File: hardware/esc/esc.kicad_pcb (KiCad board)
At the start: 2 copper layers, 214 parts, among them J1 TO_FC, J10 PHASE_A, J11 PHASE_B, J12 PHASE_C, J13 PHASE_A, J14 PHASE_B, J15 PHASE_C, J2 BAT_IN, J3 BAT_GND, J4 PHASE_A, J5 PHASE_B, J6 PHASE_C, J7 PHASE_A, J8 PHASE_B, J9 PHASE_C, Q1 NVTFWS003N04XMTAG, Q10 NVTFWS003N04XMTAG, Q11 NVTFWS003N04XMTAG, Q12 NVTFWS003N04XMTAG, Q13 NVTFWS003N04XMTAG, Q14 NVTFWS003N04XMTAG, Q15 NVTFWS003N04XMTAG, Q16 NVTFWS003N04XMTAG, Q17 NVTFWS003N04XMTAG, Q18 NVTFWS003N04XMTAG, Q19 NVTFWS003N04XMTAG, Q2 NVTFWS003N04XMTAG, Q20 NVTFWS003N04XMTAG, Q21 NVTFWS003N04XMTAG, Q22 NVTFWS003N04XMTAG, Q23 NVTFWS003N04XMTAG, Q24 NVTFWS003N04XMTAG, Q3 NVTFWS003N04XMTAG, Q4 NVTFWS003N04XMTAG, Q5 NVTFWS003N04XMTAG, Q6 NVTFWS003N04XMTAG, Q7 NVTFWS003N04XMTAG, Q8 NVTFWS003N04XMTAG, Q9 NVTFWS003N04XMTAG, U1 DRV8300DRGER, U10 DRV8300DRGER, U11 STM32G071K8U6, U12 INA180A1, U13 TPS56339DDC, U14 NCP59800BMNADJTAG, U2 STM32G071K8U6, U3 INA180A1, U4 DRV8300DRGER, U5 STM32G071K8U6, U6 INA180A1, U7 DRV8300DRGER, U8 STM32G071K8U6, U9 INA180A1

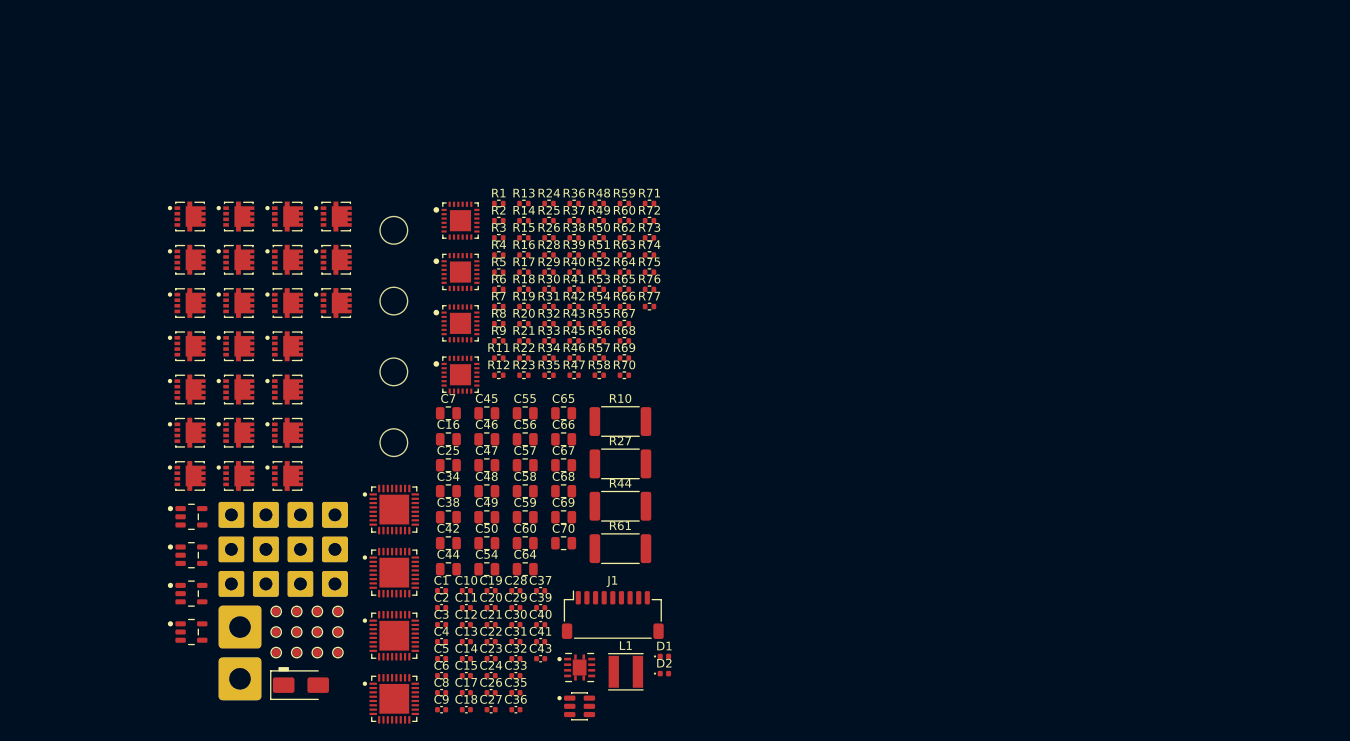
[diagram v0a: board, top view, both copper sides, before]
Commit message: h/feat: gate drive routing + prelim layout
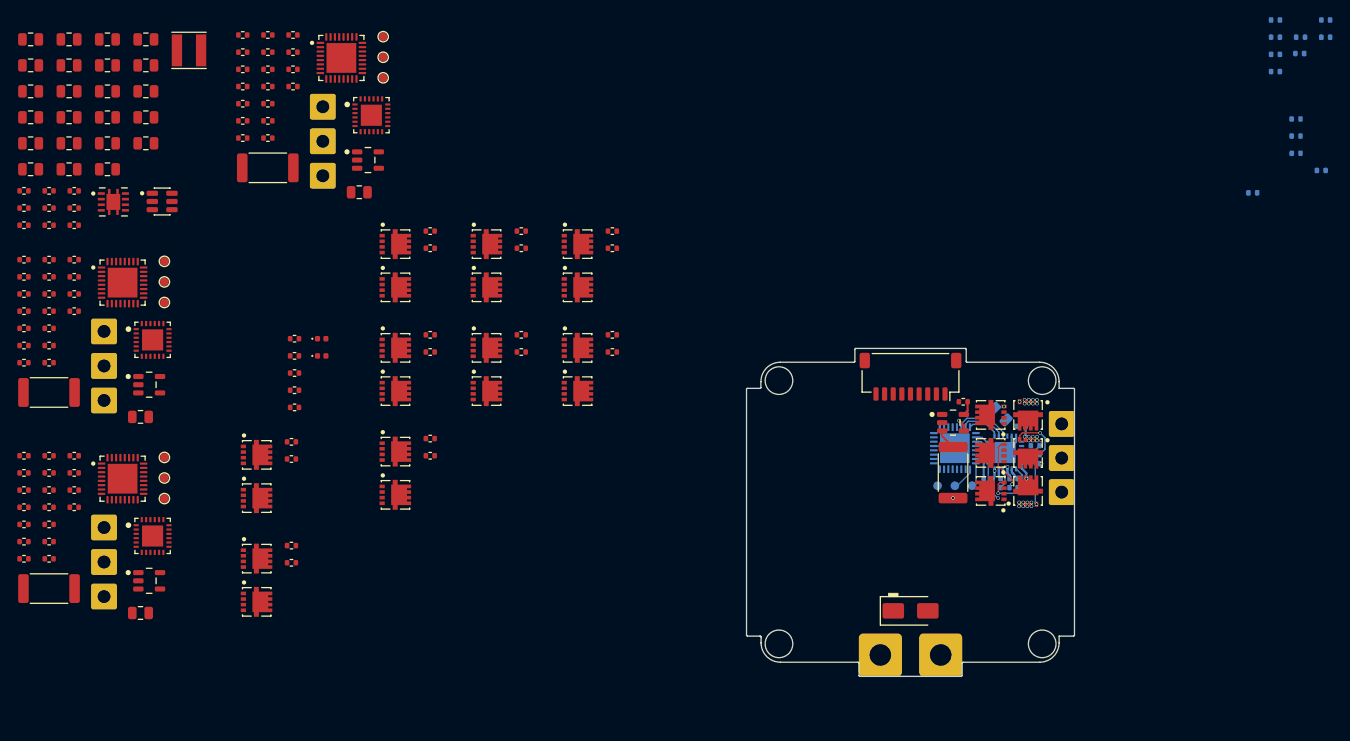
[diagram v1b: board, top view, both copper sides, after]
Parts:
- C1, C10, C19, C2, C20, C21, C22, C23, C24, C26, C27, C28, C29, C3, C30, C31, C32, C33, C35, C36, C37, C39, C4, C40, C41, C43, C5, C6, C8, C9: footprint Capacitor_SMD:C_0402_1005Metric -> Stratus:C_0402
- C11, C12, C13, C14, C15, C17, C18: footprint Capacitor_SMD:C_0402_1005Metric -> Stratus:C_0402; moved to B.Cu
- C16, TP5, TP6, TP7, U4, U5: moved to B.Cu
- R1, R11, R12, R13, R14, R15, R2, R3, R39, R4, R40, R41, R42, R43, R45, R46, R47, R48, R49, R5, R56, R57, R58, R59, R6, R60, R62, R63, R64, R65, R66, R7, R73, R74, R75, R76, R77, R8, R9: footprint Resistor_SMD:R_0402_1005Metric -> Stratus:R_0402
- R16, R17, R18, R19, R20, R21, R50, R51, R52, R53, R54, R55, R67, R68, R69, R70, R71, R72: value 10R -> 24R; footprint Resistor_SMD:R_0402_1005Metric -> Stratus:R_0402
- R22, R23, R24, R25, R26, R28, R29, R30, R31, R32: footprint Resistor_SMD:R_0402_1005Metric -> Stratus:R_0402; moved to B.Cu
- R33, R34, R35, R36, R37, R38: value 10R -> 24R; footprint Resistor_SMD:R_0402_1005Metric -> Stratus:R_0402; moved to B.Cu
- moved C11 120.6 mm to (214.5, 34.6), turned to 180 degrees
- moved C12 120.6 mm to (214.5, 36.6), turned to 180 degrees
- moved C18 117.1 mm to (214.0, 52.0), turned to 180 degrees
- moved R22 97.4 mm to (211.6, 36.6), turned to 180 degrees
- moved R23 97.3 mm to (211.5, 38.5), turned to 180 degrees
- moved Q8 95.5 mm to (180.0, 84.7), turned to -90 degrees
- moved Q10 94.0 mm to (180.0, 89.1), turned to 90 degrees
- moved J9 92.8 mm to (183.9, 89.3)
- moved J8 92.8 mm to (183.9, 85.3)
- moved J7 92.8 mm to (183.9, 81.4)
- moved Q7 92.8 mm to (175.7, 84.7), turned to 180 degrees
- moved Q12 91.5 mm to (180.0, 80.3), turned to -90 degrees
- moved Q9 91.1 mm to (175.7, 89.1), turned to 180 degrees
- moved U6 89.6 mm to (171.3, 81.2)
- moved R29 89.1 mm to (208.7, 34.6), turned to 180 degrees
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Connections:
- Q1 pad 5_6_7_8: (no net) -> /ESC Module 1/V_FET
- Q10 pad 5_6_7_8: (no net) -> /ESC Module 2/PHASE_C
- Q11 pad 5_6_7_8: (no net) -> /ESC Module 2/V_FET
- Q12 pad 5_6_7_8: (no net) -> /ESC Module 2/PHASE_A
- Q13 pad 5_6_7_8: (no net) -> /ESC Module 3/V_FET
- Q14 pad 5_6_7_8: (no net) -> /ESC Module 3/PHASE_B
- Q15 pad 5_6_7_8: (no net) -> /ESC Module 3/V_FET
- Q16 pad 5_6_7_8: (no net) -> /ESC Module 3/PHASE_C
- Q17 pad 5_6_7_8: (no net) -> /ESC Module 3/V_FET
- Q18 pad 5_6_7_8: (no net) -> /ESC Module 3/PHASE_A
- Q19 pad 5_6_7_8: (no net) -> /ESC Module 4/V_FET
- Q2 pad 5_6_7_8: (no net) -> /ESC Module 1/PHASE_A
- Q20 pad 5_6_7_8: (no net) -> /ESC Module 4/PHASE_B
- Q21 pad 5_6_7_8: (no net) -> /ESC Module 4/V_FET
- Q22 pad 5_6_7_8: (no net) -> /ESC Module 4/PHASE_C
- Q23 pad 5_6_7_8: (no net) -> /ESC Module 4/V_FET
- Q24 pad 5_6_7_8: (no net) -> /ESC Module 4/PHASE_A
- Q3 pad 5_6_7_8: (no net) -> /ESC Module 1/V_FET
- Q4 pad 5_6_7_8: (no net) -> /ESC Module 1/PHASE_B
- Q5 pad 5_6_7_8: (no net) -> /ESC Module 1/V_FET
- Q6 pad 5_6_7_8: (no net) -> /ESC Module 1/PHASE_C
- Q7 pad 5_6_7_8: (no net) -> /ESC Module 2/V_FET
- Q8 pad 5_6_7_8: (no net) -> /ESC Module 2/PHASE_B
- Q9 pad 5_6_7_8: (no net) -> /ESC Module 2/V_FET
- U11 pad 14: /ESC Module 4/LA -> /ESC Module 4/LC
- U11 pad 16: /ESC Module 4/LC -> /ESC Module 4/LA
- U2 pad 14: /ESC Module 1/LA -> /ESC Module 1/LC
- U2 pad 16: /ESC Module 1/LC -> /ESC Module 1/LA
- U5 pad 14: /ESC Module 2/LA -> /ESC Module 2/LC
- U5 pad 16: /ESC Module 2/LC -> /ESC Module 2/LA
- U8 pad 14: /ESC Module 3/LA -> /ESC Module 3/LC
- U8 pad 16: /ESC Module 3/LC -> /ESC Module 3/LA
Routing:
- net Net-(Q11-G): track 0.00 -> 12.5 mm, vias 0 -> 2
- net /ESC Module 2/V_FET: track 0.00 -> 10.7 mm, vias 0 -> 2
- net GND: track 0.00 -> 10.4 mm, vias 0 -> 24
- net Net-(Q12-G): track 0.00 -> 8.46 mm, vias 0 -> 2
- net Net-(Q10-G): track 0.00 -> 7.07 mm, vias 0 -> 1
- net /ESC Module 2/LC: track 0.00 -> 6.62 mm
- net Net-(Q7-G): track 0.00 -> 6.27 mm, vias 0 -> 1
- net Net-(Q8-G): track 0.00 -> 5.98 mm, vias 0 -> 1
- net Net-(Q9-G): track 0.00 -> 5.36 mm, vias 0 -> 1
- net /ESC Module 2/LB: track 0.00 -> 5.32 mm
- net /ESC Module 2/LA: track 0.00 -> 3.79 mm
- net /ESC Module 2/GHA: track 0.00 -> 3.06 mm
- net Net-(U4-BSTA): track 0.00 -> 2.81 mm
- net /ESC Module 2/SWCLK: track 0.00 -> 2.80 mm
- net /ESC Module 2/SWDIO: track 0.00 -> 2.78 mm
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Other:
- board outline added: 38 x 38 mm
- copper layers 2 -> 8

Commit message: h/fix: update schematic to better match AM32 hardware groups; further layout work
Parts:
- moved C11 68.8 mm to (167.4, 84.7)
- moved C12 68.1 mm to (167.4, 85.7)
- moved R22 64.6 mm to (167.4, 83.7)
- moved C18 55.8 mm to (167.4, 82.6)
- moved R30 39.5 mm to (180.7, 64.3), turned to -90 degrees
- moved R23 38.7 mm to (182.7, 64.3), turned to 90 degrees
- moved R29 36.9 mm to (186.9, 64.3), turned to -90 degrees
- moved R24 34.6 mm to (181.7, 64.3), turned to 90 degrees
- moved R31 34.4 mm to (185.8, 64.3), turned to -90 degrees
- moved R25 30.9 mm to (184.8, 64.3), turned to 90 degrees
- moved R32 30.9 mm to (189.0, 64.3), turned to -90 degrees
- moved R26 30.9 mm to (183.8, 64.3), turned to -90 degrees
- moved R28 20.6 mm to (187.9, 64.3), turned to 90 degrees
- moved C16 1.27 mm to (178.1, 80.4), turned to 90 degrees
- moved C15 0.84 mm to (180.1, 81.7)
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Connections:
- U11 pad 12: /ESC Module 4/VIRTUAL -> /ESC Module 4/SNS_CURR
- U11 pad 8: /ESC Module 4/SNS_CURR -> /ESC Module 4/VIRTUAL
- U2 pad 12: /ESC Module 1/VIRTUAL -> /ESC Module 1/SNS_CURR
- U2 pad 8: /ESC Module 1/SNS_CURR -> /ESC Module 1/VIRTUAL
- U5 pad 12: /ESC Module 2/VIRTUAL -> /ESC Module 2/SNS_CURR
- U5 pad 8: /ESC Module 2/SNS_CURR -> /ESC Module 2/VIRTUAL
- U8 pad 12: /ESC Module 3/VIRTUAL -> /ESC Module 3/SNS_CURR
- U8 pad 8: /ESC Module 3/SNS_CURR -> /ESC Module 3/VIRTUAL
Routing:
- net /ESC Module 2/SWDIO: track 2.78 -> 0.00 mm
- net /ESC Module 2/SWCLK: track 2.80 -> 0.28 mm
- net /ESC Module 2/BEMF_B: track 0.00 -> 2.19 mm
- net /ESC Module 2/BEMF_C: track 0.00 -> 2.08 mm
- net /ESC Module 2/V_FET: track 10.7 -> 9.27 mm, vias 2 -> 1
- net GND: track 10.4 -> 9.17 mm
- net /ESC Module 2/nRST: track 0.00 -> 1.04 mm
- net Net-(Q11-G): vias 2 -> 1

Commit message: h/feat: placement
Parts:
- moved R24 27.3 mm to (168.7, 88.3)
- moved R31 27.3 mm to (172.9, 88.3), turned to 90 degrees
- moved R23 26.8 mm to (170.8, 88.3), turned to -90 degrees
- moved R26 26.8 mm to (171.8, 88.3), turned to 90 degrees
- moved R30 26.4 mm to (169.8, 88.3), turned to 90 degrees
- moved R25 26.4 mm to (173.9, 88.3), turned to -90 degrees
- moved R28 25.4 mm to (168.0, 80.0)
- moved R29 25.4 mm to (166.9, 80.0)
- moved R32 25.4 mm to (169.0, 80.0)
- moved TP5 8.74 mm to (170.4, 79.8)
- moved TP6 8.74 mm to (174.4, 79.8)
- moved TP7 8.74 mm to (172.4, 79.8)
- moved C16 1.18 mm to (176.9, 80.2), turned to 135 degrees
- moved C15 0.62 mm to (179.5, 81.7)
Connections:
- U11 pad 10: /ESC Module 4/BEMF_B -> /ESC Module 4/VIRTUAL
- U11 pad 11: /ESC Module 4/BEMF_C -> unconnected-(U11-PA4-Pad11)
- U11 pad 13: unconnected-(U11-PA6-Pad13) -> SNS_BAT
- U11 pad 26: /M4 -> unconnected-(U11-PA15-Pad26)
- U11 pad 27: unconnected-(U11-PB3-Pad27) -> /ESC Module 4/BEMF_B
- U11 pad 28: unconnected-(U11-PB4-Pad28) -> /M4
- U11 pad 31: unconnected-(U11-PB7-Pad31) -> /ESC Module 4/BEMF_A
- U11 pad 7: SNS_BAT -> unconnected-(U11-PA0-Pad7)
- U11 pad 8: /ESC Module 4/VIRTUAL -> unconnected-(U11-PA1-Pad8)
- U11 pad 9: /ESC Module 4/BEMF_A -> /ESC Module 4/BEMF_C
- U2 pad 10: /ESC Module 1/BEMF_B -> /ESC Module 1/VIRTUAL
- U2 pad 11: /ESC Module 1/BEMF_C -> unconnected-(U2-PA4-Pad11)
- U2 pad 13: unconnected-(U2-PA6-Pad13) -> SNS_BAT
- U2 pad 26: /M1 -> unconnected-(U2-PA15-Pad26)
- U2 pad 27: unconnected-(U2-PB3-Pad27) -> /ESC Module 1/BEMF_B
- U2 pad 28: unconnected-(U2-PB4-Pad28) -> /M1
- U2 pad 31: unconnected-(U2-PB7-Pad31) -> /ESC Module 1/BEMF_A
- U2 pad 7: SNS_BAT -> unconnected-(U2-PA0-Pad7)
- U2 pad 8: /ESC Module 1/VIRTUAL -> unconnected-(U2-PA1-Pad8)
- U2 pad 9: /ESC Module 1/BEMF_A -> /ESC Module 1/BEMF_C
- U5 pad 10: /ESC Module 2/BEMF_B -> /ESC Module 2/VIRTUAL
- U5 pad 11: /ESC Module 2/BEMF_C -> unconnected-(U5-PA4-Pad11)
- U5 pad 13: unconnected-(U5-PA6-Pad13) -> SNS_BAT
- U5 pad 26: /M2 -> unconnected-(U5-PA15-Pad26)
- U5 pad 27: unconnected-(U5-PB3-Pad27) -> /ESC Module 2/BEMF_B
- U5 pad 28: unconnected-(U5-PB4-Pad28) -> /M2
- U5 pad 31: unconnected-(U5-PB7-Pad31) -> /ESC Module 2/BEMF_A
- U5 pad 7: SNS_BAT -> unconnected-(U5-PA0-Pad7)
- U5 pad 8: /ESC Module 2/VIRTUAL -> unconnected-(U5-PA1-Pad8)
- U5 pad 9: /ESC Module 2/BEMF_A -> /ESC Module 2/BEMF_C
- U8 pad 10: /ESC Module 3/BEMF_B -> /ESC Module 3/VIRTUAL
- U8 pad 11: /ESC Module 3/BEMF_C -> unconnected-(U8-PA4-Pad11)
- U8 pad 13: unconnected-(U8-PA6-Pad13) -> SNS_BAT
- U8 pad 26: /M3 -> unconnected-(U8-PA15-Pad26)
- U8 pad 27: unconnected-(U8-PB3-Pad27) -> /ESC Module 3/BEMF_B
- U8 pad 28: unconnected-(U8-PB4-Pad28) -> /M3
- U8 pad 31: unconnected-(U8-PB7-Pad31) -> /ESC Module 3/BEMF_A
- U8 pad 7: SNS_BAT -> unconnected-(U8-PA0-Pad7)
- U8 pad 8: /ESC Module 3/VIRTUAL -> unconnected-(U8-PA1-Pad8)
- U8 pad 9: /ESC Module 3/BEMF_A -> /ESC Module 3/BEMF_C
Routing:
- net /ESC Module 2/V_FET: track 9.27 -> 0.00 mm, vias 1 -> 0
- net /ESC Module 2/VIRTUAL: track 0.00 -> 7.26 mm, vias 0 -> 2
- net /ESC Module 2/BEMF_A: track 0.00 -> 3.52 mm
- net /ESC Module 2/BEMF_C: track 2.08 -> 3.62 mm
- net V_3V3: track 1.65 -> 3.11 mm
- net /ESC Module 2/BEMF_B: track 2.19 -> 3.54 mm
- net /ESC Module 2/nRST: track 1.04 -> 2.35 mm, vias 0 -> 1
- net /M2: track 0.00 -> 0.01 mm, vias 0 -> 1
- net TELEM: vias 0 -> 1

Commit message: h/feat: layout - 1/4 motors
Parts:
- removed C65, C66, C67, C68, C69, C70: 10uF, Capacitor_SMD:C_0805_2012Metric
- added C73: 10uF, Capacitor_SMD:C_0805_2012Metric, F.Cu at (173.9, 76.3)
- added C74: 10uF, Capacitor_SMD:C_0805_2012Metric, F.Cu at (176.2, 76.3)
- added C75: 10uF, Capacitor_SMD:C_0805_2012Metric, F.Cu at (178.4, 76.3)
- added C76: 10uF, Capacitor_SMD:C_0805_2012Metric, F.Cu at (134.6, 97.3)
- added C77: 10uF, Capacitor_SMD:C_0805_2012Metric, F.Cu at (134.6, 100.3)
- added C78: 10uF, Capacitor_SMD:C_0805_2012Metric, F.Cu at (134.6, 103.3)
- added C79: 10uF, Capacitor_SMD:C_0805_2012Metric, F.Cu at (128.2, 108.3)
- added C80: 10uF, Capacitor_SMD:C_0805_2012Metric, F.Cu at (128.2, 111.3)
- added C81: 10uF, Capacitor_SMD:C_0805_2012Metric, F.Cu at (128.2, 114.3)
- C1, R2, R4: moved to B.Cu
- moved C58 111.4 mm to (167.5, 99.4), turned to 90 degrees
- moved C48 111.3 mm to (167.5, 88.4), turned to -90 degrees
- moved C57 111.2 mm to (165.3, 99.4), turned to 90 degrees
- moved C55 109.2 mm to (167.5, 95.7), turned to -90 degrees
- moved C45 108.9 mm to (167.5, 81.1), turned to -90 degrees
- moved C54 108.9 mm to (167.5, 92.1), turned to 90 degrees
- moved C50 108.2 mm to (165.3, 92.1), turned to 90 degrees
- moved C47 108.2 mm to (167.5, 84.8), turned to 90 degrees
- moved C49 107.9 mm to (165.3, 88.4), turned to -90 degrees
- moved C44 107.9 mm to (165.3, 81.1), turned to -90 degrees
- moved C46 107.0 mm to (165.3, 84.8), turned to 90 degrees
- moved C56 105.9 mm to (165.3, 95.7), turned to -90 degrees
- moved C59 77.3 mm to (128.2, 97.3)
- moved C60 77.3 mm to (128.2, 100.3)
- moved C64 77.3 mm to (128.2, 103.3)
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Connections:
- C59 pad 1: V_BAT -> /ESC Module 1/V_FET
- C60 pad 1: V_BAT -> /ESC Module 1/V_FET
- C64 pad 1: V_BAT -> /ESC Module 1/V_FET
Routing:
- net SNS_BAT: track 0.00 -> 18.1 mm, vias 0 -> 2
- net /ESC Module 2/PHASE_A: track 1.46 -> 17.2 mm, vias 1 -> 3
- net /ESC Module 2/PHASE_C: track 2.01 -> 16.2 mm, vias 1 -> 2
- net /ESC Module 2/VIRTUAL: track 7.26 -> 18.9 mm
- net TELEM: track 0.00 -> 11.4 mm, vias 1 -> 2
- net /M2: track 0.01 -> 11.3 mm, vias 1 -> 2
- net /ESC Module 2/V_FET: track 0.00 -> 10.5 mm, vias 0 -> 2
- net /ESC Module 2/SWDIO: track 0.00 -> 7.87 mm, vias 0 -> 2
- net /ESC Module 2/SWCLK: track 0.00 -> 7.62 mm, vias 0 -> 2
- net /ESC Module 2/PHASE_B: track 1.71 -> 9.31 mm, vias 1 -> 2
- net /ESC Module 2/nRST: track 2.35 -> 8.26 mm, vias 1 -> 2
- net /ESC Module 2/SNS_CURR: track 0.00 -> 3.04 mm, vias 0 -> 1
- net /ESC Module 2/GLC: track 0.00 -> 1.28 mm
- net Net-(Q11-G): track 12.5 -> 13.6 mm, vias 1 -> 2
- net GND: track 9.17 -> 10.2 mm, vias 24 -> 37
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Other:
- copper layers 8 -> 6
- board text added: "V_S"

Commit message: h/feat: layout
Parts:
- added C61: 10uF, Capacitor_SMD:C_0805_2012Metric, F.Cu at (167.5, 103.0)
- added C62: 10uF, Capacitor_SMD:C_0805_2012Metric, F.Cu at (165.3, 103.0)
- added J7: PHASE_A, Stratus:Phase_Pad_3x3_D1.5, F.Cu at (183.9, 93.9)
- added J8: PHASE_B, Stratus:Phase_Pad_3x3_D1.5, F.Cu at (183.9, 97.9)
- added J9: PHASE_C, Stratus:Phase_Pad_3x3_D1.5, F.Cu at (183.9, 101.8)
- added REF**: C_0603_1608Metric, Capacitor_SMD:C_0603_1608Metric, B.Cu at (145.2, 95.6)
- added REF**: C_0603_1608Metric, Capacitor_SMD:C_0603_1608Metric, B.Cu at (142.1, 95.6)
- C38, C39, C42, L1, R73, R75, R77, U13: moved to B.Cu
- moved C38 90.5 mm to (129.7, 99.5), turned to 180 degrees
- moved R75 88.6 mm to (140.2, 107.7), turned to 180 degrees
- moved C42 86.7 mm to (131.3, 95.1), turned to 180 degrees
- moved L1 85.9 mm to (143.7, 98.8)
- moved C39 82.1 mm to (133.3, 98.0), turned to 180 degrees
- moved R77 81.0 mm to (135.0, 106.1), turned to 180 degrees
- moved R73 78.7 mm to (132.6, 99.2), turned to 180 degrees
- moved U13 73.0 mm to (132.3, 106.2), turned to -90 degrees
- moved C1 25.7 mm to (189.7, 82.9)
- moved R2 25.7 mm to (191.2, 83.5)
- moved R4 25.7 mm to (191.2, 82.4)
- moved D3 3.65 mm to (166.4, 106.7)
- moved J2 3.47 mm to (162.9, 111.6)
- moved J3 3.47 mm to (169.9, 111.6)
- moved C12 1.04 mm to (167.4, 83.9)
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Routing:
- net SNS_BAT: track 18.1 -> 15.9 mm, vias 2 -> 1
- net V_3V3: track 3.11 -> 1.46 mm
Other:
- board size 38 x 38 mm -> 38 x 41.5 mm

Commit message: h/feat: power stage placement
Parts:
- removed REF** (x2): C_0603_1608Metric, Capacitor_SMD:C_0603_1608Metric
- added C13: 1uF, Capacitor_SMD:C_0402_1005Metric, B.Cu at (169.7, 105.3)
- added C6: 10nF, Capacitor_SMD:C_0402_1005Metric, B.Cu at (169.7, 107.2)
- added C65: 22uF, Capacitor_SMD:C_0805_2012Metric, B.Cu at (166.4, 101.7)
- added R4: 31.6k, Resistor_SMD:R_0402_1005Metric, B.Cu at (176.0, 107.5)
- added R5: 10k, Resistor_SMD:R_0402_1005Metric, B.Cu at (174.9, 107.5)
- added U2: NCP59800BMNADJTAG, Stratus:NCP59800BMNADJTAG, B.Cu at (172.3, 106.4)
- C40: value 4.7uF -> 22uF; footprint Stratus:C_0402 -> Capacitor_SMD:C_0603_1608Metric; moved to B.Cu
- moved C40 122.6 mm to (175.9, 105.8), turned to 180 degrees
- moved C42 40.0 mm to (170.5, 103.3), turned to 0 degrees
- moved C38 32.4 mm to (161.9, 103.3)
- moved R77 30.5 mm to (165.5, 108.0)
- moved U13 29.7 mm to (161.9, 106.4)
- moved R73 27.8 mm to (159.2, 107.5), turned to 0 degrees
- moved C39 27.3 mm to (159.2, 106.4), turned to 0 degrees
- moved R75 27.2 mm to (167.4, 108.0)
- moved L1 23.6 mm to (166.4, 105.0)
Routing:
- net GND: track 10.0 -> 13.4 mm, vias 37 -> 38
- net Net-(U2-FB/SNS): track 0.00 -> 2.81 mm
- net V_3V3: track 1.46 -> 3.05 mm
- net Net-(U2-NR): track 0.00 -> 1.22 mm
- net Net-(C39-Pad1): track 0.00 -> 1.04 mm
- net V_5V: vias 2 -> 3
- added copper zone on B.Cu, net V_3V3

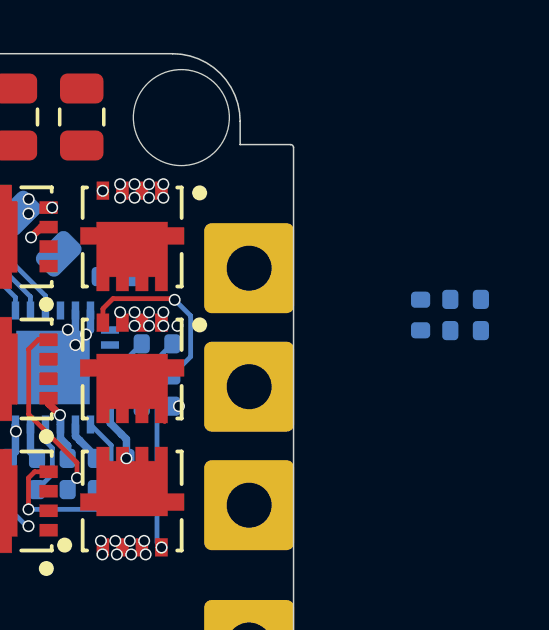
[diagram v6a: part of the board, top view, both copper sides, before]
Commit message: h/fix: move v_bat sensing to FC
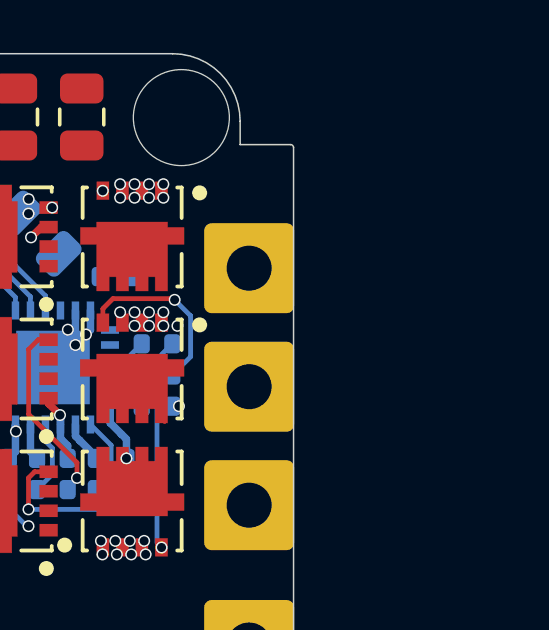
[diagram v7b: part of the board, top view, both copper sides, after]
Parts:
- removed C1: 0.1uF, Stratus:C_0402
- removed R2: 56k, Stratus:R_0402
- removed the R4 at (191.2, 82.4)
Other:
- board text removed: "V_S"
